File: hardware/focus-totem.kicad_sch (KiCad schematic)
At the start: 13 parts, among them J1 SSD1306_0.91, SW1 SW_Push, SW2 SW_Push, SW3 SW_Push, SW4 EC11, U1 XIAO-RP2040

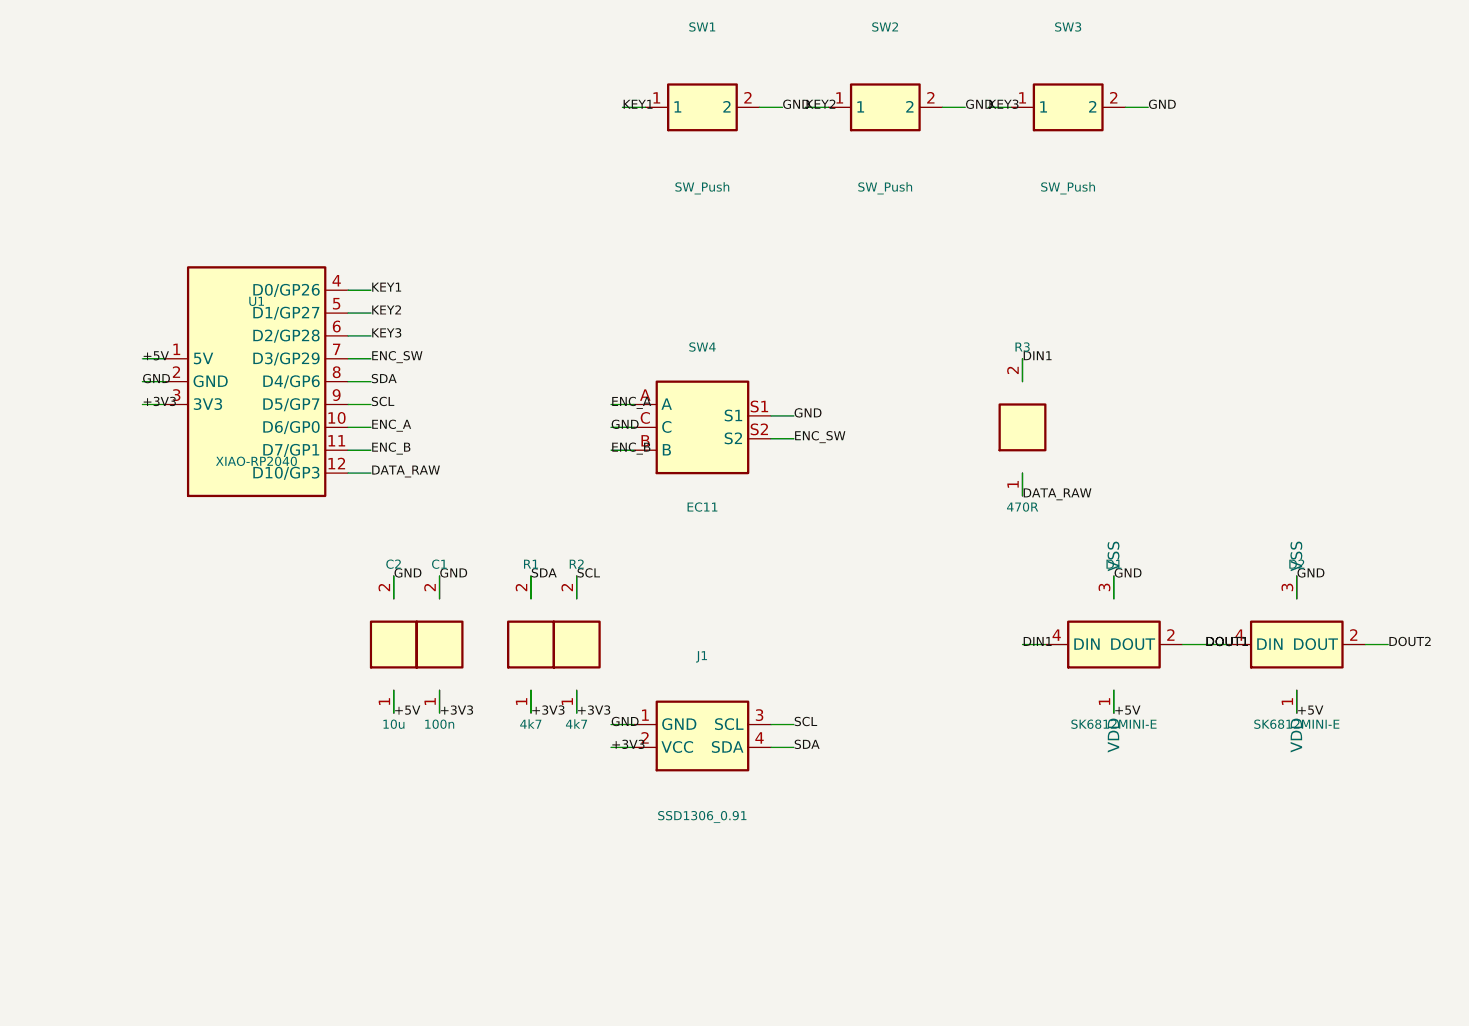
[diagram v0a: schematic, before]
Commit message: Added Pomodoro timer, RGB/OLED, and updates
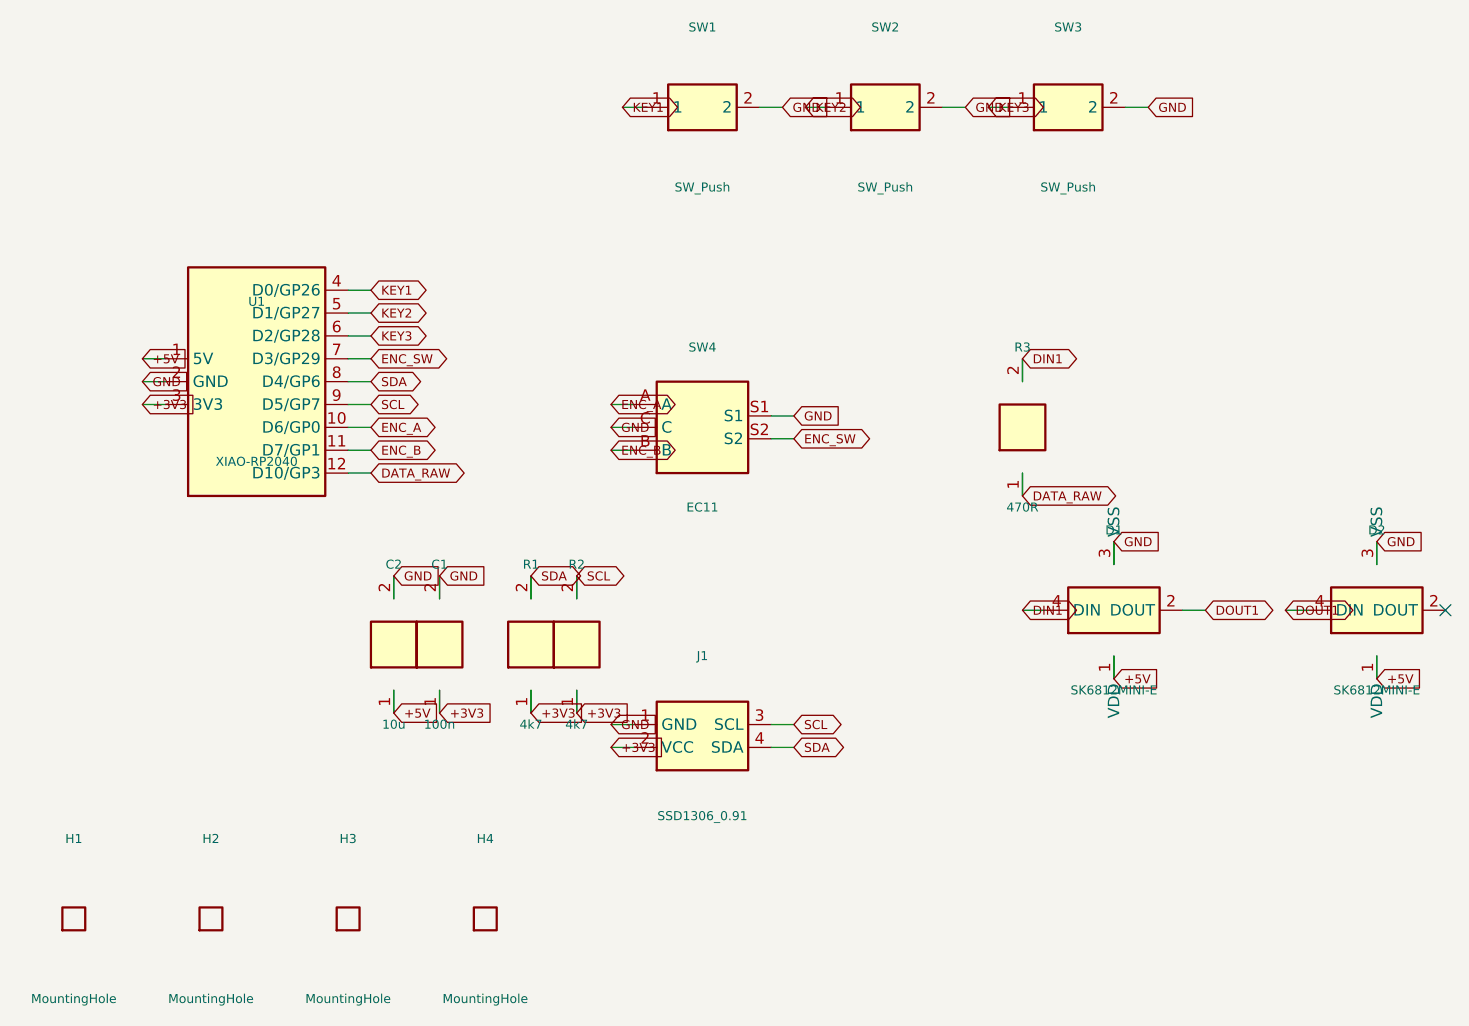
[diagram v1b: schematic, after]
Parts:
- added H1, H2, H3, H4: MountingHole, MountingHole:MountingHole_3.2mm_M3, symbol ft:MH
- D1, D2: footprint SK6812MINI-E:SK6812MINI-E -> focus-totem:SK6812MINI-E
- SW1, SW2, SW3: footprint Button_Switch_Keyboard:SW_Cherry_MX_1.00u -> Button_Switch_Keyboard:SW_Cherry_MX_1.00u_PCB
- SW4: footprint Rotary_Encoder:RotaryEncoder_Alps_EC11E-Switch -> Rotary_Encoder:RotaryEncoder_Alps_EC11E-Switch_Vertical_H20mm
- U1: footprint XIAO-RP2040:XIAO-RP2040 -> focus-totem:XIAO-RP2040
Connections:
- net DOUT2: no longer names the net of D2.2 (DOUT)
- no-connect marks 0 -> 1
